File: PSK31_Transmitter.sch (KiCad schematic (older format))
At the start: 30 parts

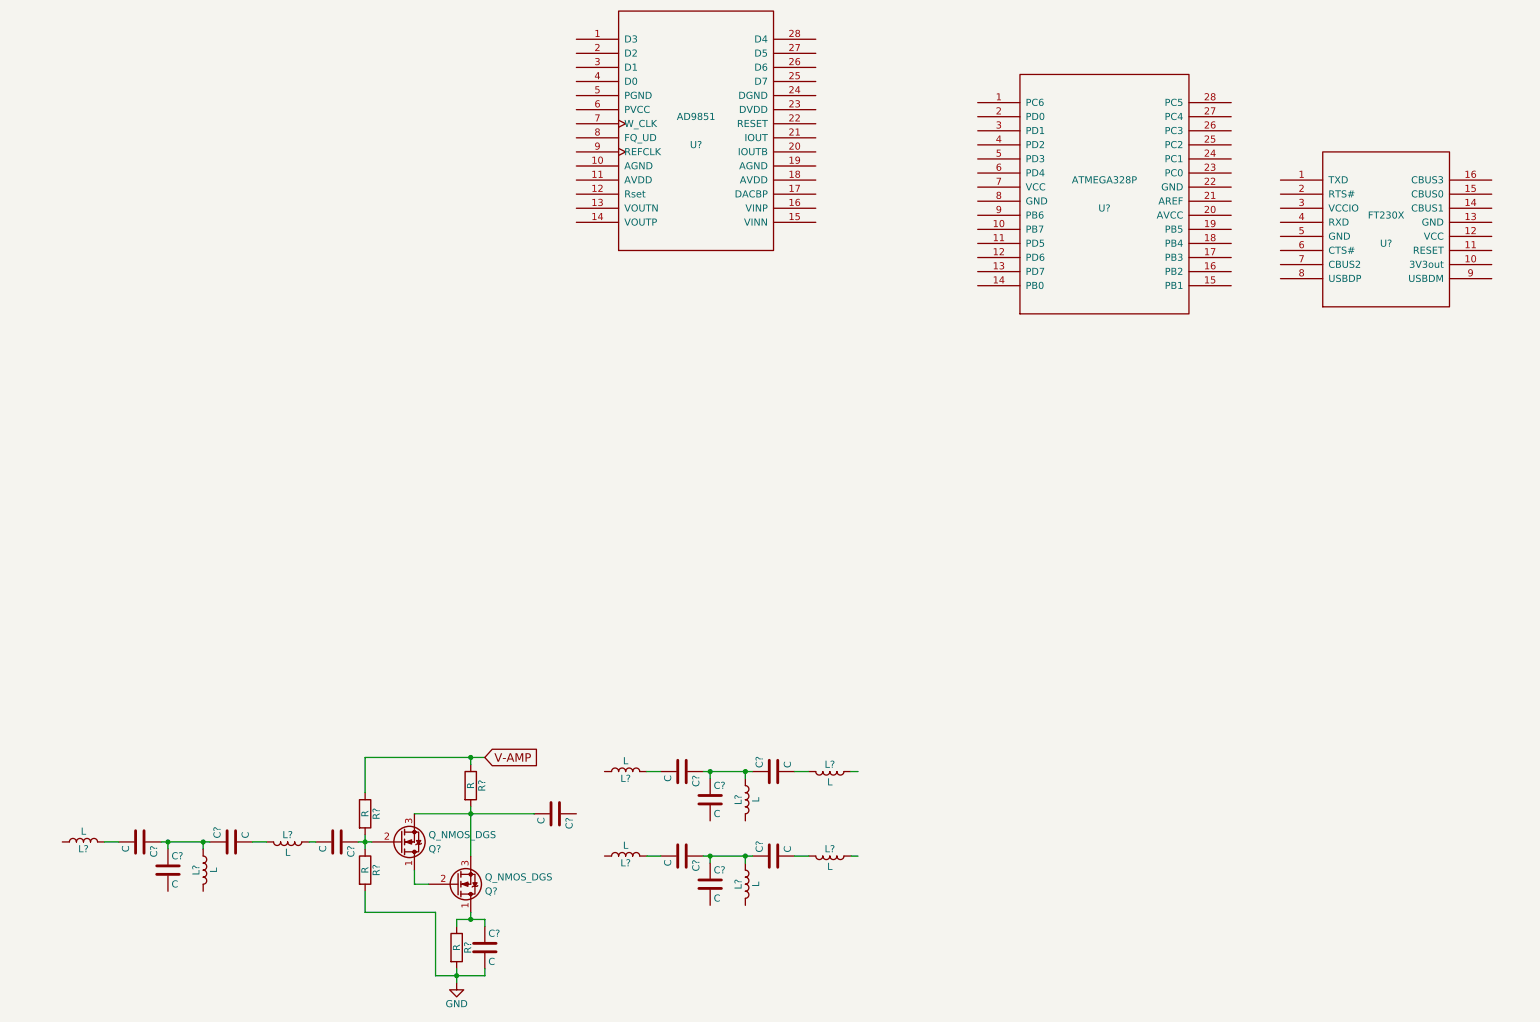
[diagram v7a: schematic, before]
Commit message: Add ftdi support circuitry and connect dds to mcu
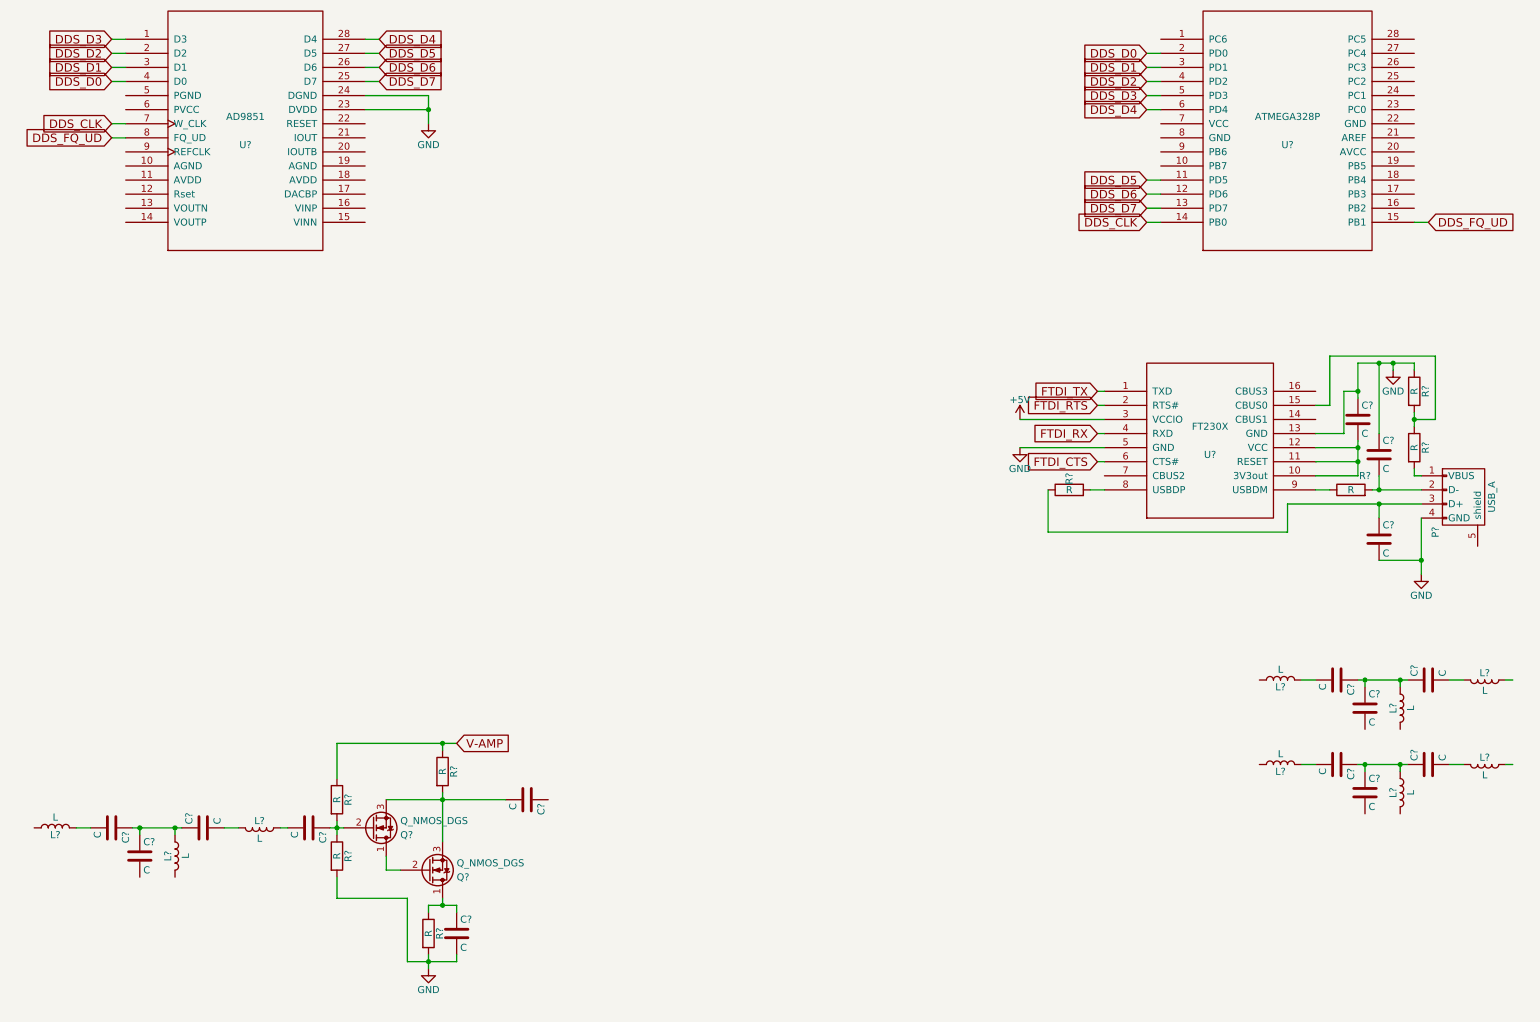
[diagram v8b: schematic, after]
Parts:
- added C? (x3): C, symbol C
- added P?: USB_A, symbol USB_A
- added R? (x4): R, symbol R
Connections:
- net labels added: +5V, DDS_CLK, DDS_D0, DDS_D1, DDS_D2, DDS_D3, DDS_D4, DDS_D5, DDS_D6, DDS_D7, DDS_FQ_UD, FTDI_CTS, FTDI_RTS, FTDI_RX, FTDI_TX
- wire segments 37 -> 97
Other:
- moved on the sheet: C?, L?, Q?, R?, U?
